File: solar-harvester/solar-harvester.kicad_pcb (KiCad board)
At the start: 2 copper layers, 46.2 x 15.7 mm, 18 parts, among them P1 CONN_2, P2 CONN_2, P3 CONN_2, P4 CONN_6, P5 CONN_6, U1 LTC3588-1

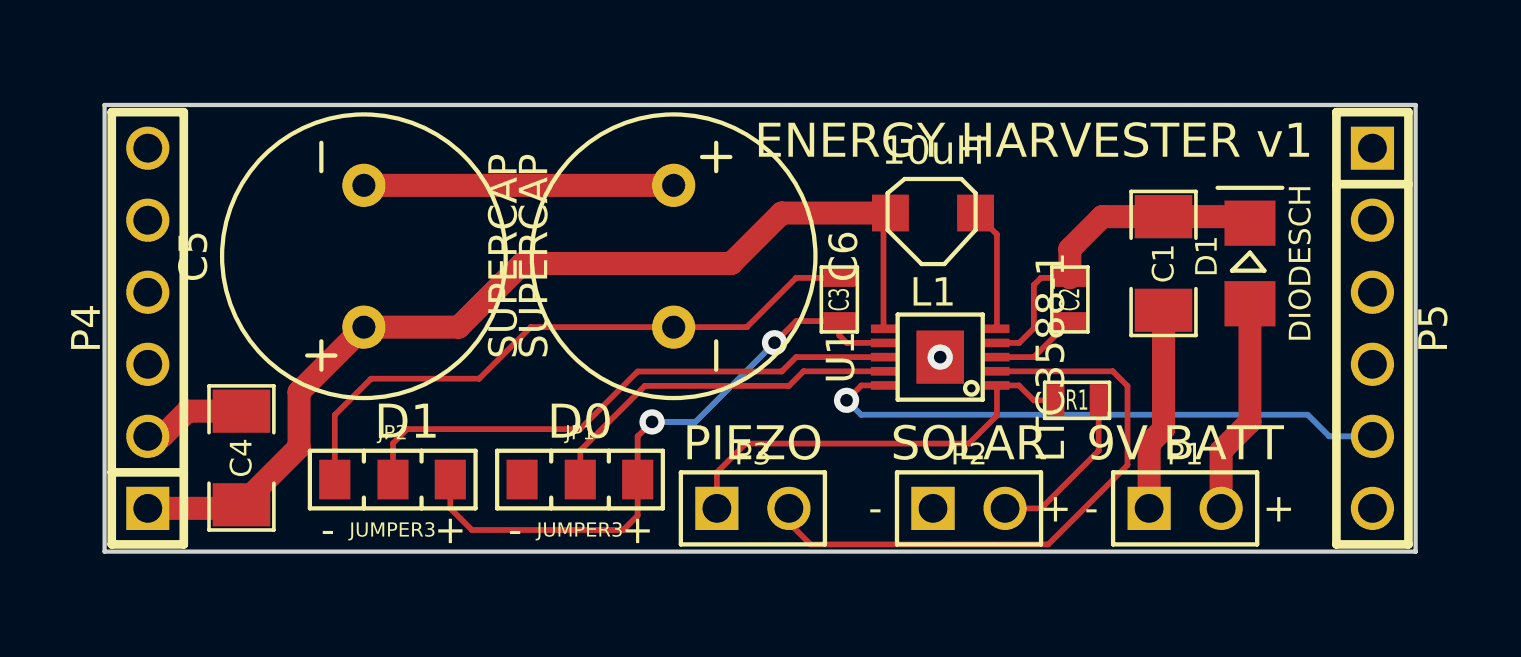
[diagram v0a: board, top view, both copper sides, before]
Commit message: solar-harvester: Add initial PCB layout.
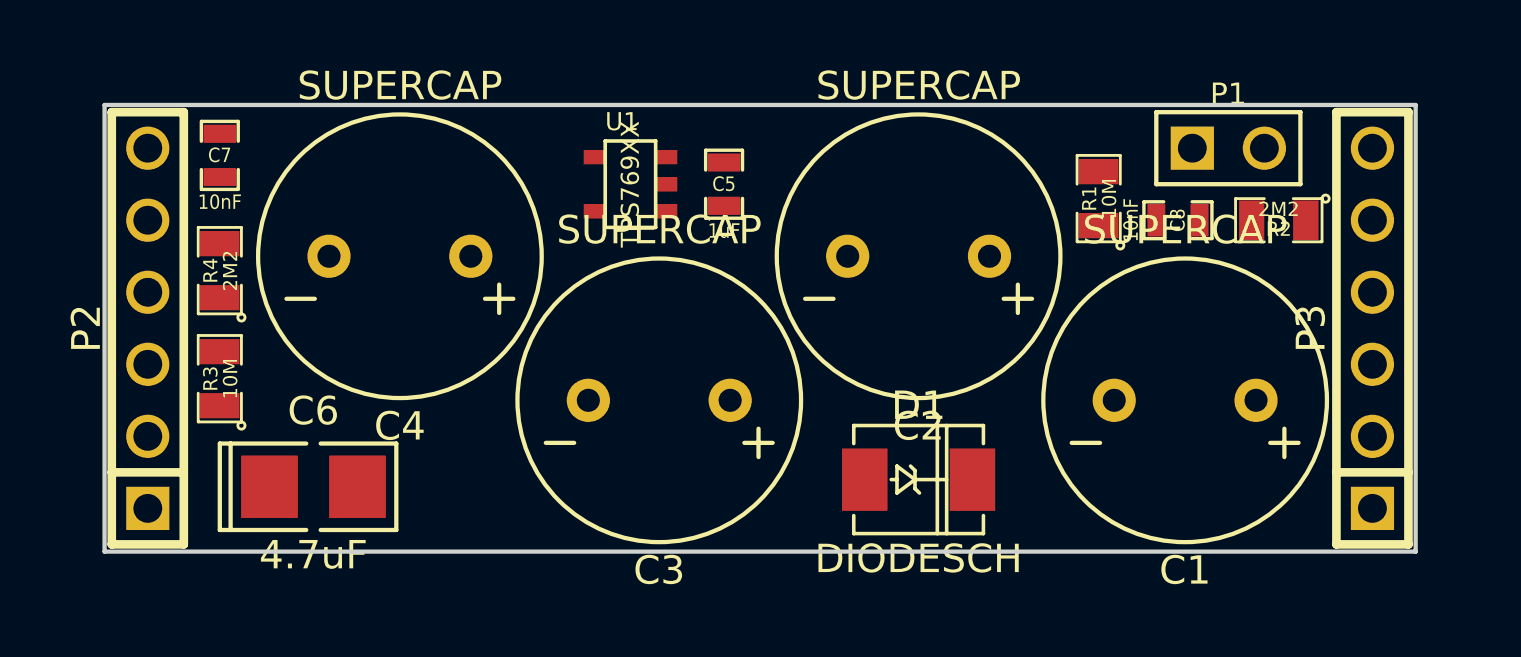
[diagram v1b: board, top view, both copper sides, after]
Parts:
- removed ?: , LOGO_SNOWCAP_BACK
- removed JP1, JP2: JUMPER3, SM0805_JUMPER3
- removed L1: 10uH, INDUCTOR-CDRH2D18-LD
- removed P4, P5: CONN_6, PIN_ARRAY-6X1
- added C7: 10nF, SM0603_Capa, F.Cu at (29.5, 40.9)
- added C8: 10nF, SM0603_Capa, F.Cu at (63.2, 43.2)
- added R2: 2M2, SM0805, F.Cu at (66.8, 43.2)
- added R3: 10M, SM0805, F.Cu at (29.5, 48.8)
- added R4: 2M2, SM0805, F.Cu at (29.5, 45.0)
- C1: value 100uF -> SUPERCAP; footprint SM1206 -> SUPERCAP_ESHSR-0010C0-002R7
- C2: value 1uF -> SUPERCAP; footprint SM0603 -> SUPERCAP_ESHSR-0010C0-002R7
- C3: value 4.7uF -> SUPERCAP; footprint SM0603 -> SUPERCAP_ESHSR-0010C0-002R7
- C4: value 10uF -> SUPERCAP; footprint SM1206 -> SUPERCAP_ESHSR-0010C0-002R7
- C5: value SUPERCAP -> 1uF; footprint SUPERCAP_ESHSR-0010C0-002R7 -> SM0603_Capa
- C6: value SUPERCAP -> 4.7uF; footprint SUPERCAP_ESHSR-0010C0-002R7 -> SM1411_POL
- D1: footprint DIODE-1206 -> DO-214AC(SMA)
- P2, P3: value CONN_2 -> CONN_6; footprint PIN_ARRAY_2X1 -> PIN_ARRAY-6X1
- R1: value 300R -> 10M; footprint SM0603 -> SM0805
- U1: value LTC3588-1 -> TPS769XX; footprint LTC3588-1-MSOP10 -> SOT23-5
- moved P2 29.6 mm to (26.9, 47.0), turned to 90 degrees
- moved P3 22.7 mm to (70.1, 47.0), turned to 90 degrees
- moved C6 15.1 mm to (32.8, 52.6), turned to 0 degrees
- moved D1 13.9 mm to (54.1, 52.3), turned to 0 degrees
- moved C5 13.0 mm to (47.2, 41.9)
- moved P1 12.8 mm to (65.0, 40.6)
- moved U1 12.5 mm to (43.9, 41.9)
- moved C4 9.04 mm to (35.8, 44.5), turned to 180 degrees
- moved C3 7.28 mm to (45.0, 49.5), turned to 180 degrees
- moved R1 7.15 mm to (60.5, 42.4), turned to 90 degrees
- moved C2 5.55 mm to (54.1, 44.5), turned to 180 degrees
- moved C1 4.89 mm to (63.5, 49.5), turned to 180 degrees
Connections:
- C1 pad 1: N-0000023 -> N-0000016
- C1 pad 2: GND -> N-0000015
- C2 pad 1: N-0000023 -> N-0000015
- C2 pad 2: N-0000018 -> N-000002
- C3 pad 1: /VIN2 -> N-000002
- C3 pad 2: GND -> N-0000017
- C4 pad 1: VCC -> N-0000017
- C5 pad 1: VCC -> N-0000016
- C5 pad 2: N-0000014 -> GND
- D1 pad 2: N-0000023 -> N-0000016
- P2 pad 1: GND -> N-0000014
- P2 pad 2: N-0000020 -> GND
- P3 pad 1: N-0000011 -> (no net)
- P3 pad 2: N-0000012 -> /V_MEASURE2
- R1 pad 1: N-0000020 -> N-0000016
- R1 pad 2: N-0000011 -> /V_MEASURE2
- U1 pad 1: N-0000011 -> N-0000016
- U1 pad 2: N-0000012 -> GND
- U1 pad 3: N-0000018 -> GND
- U1 pad 4: N-0000023 -> (no net)
- U1 pad 5: N-0000022 -> N-0000014
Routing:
- net VCC: track 35.8 -> 0.00 mm
- net GND: track 32.9 -> 0.00 mm, vias 1 -> 0
- net /VIN2: track 21.9 -> 0.00 mm, vias 2 -> 0
- net N-0000012: track 21.5 -> 0.00 mm
- net /PGOOD: track 20.6 -> 0.00 mm, vias 1 -> 0
- net N-0000013: track 19.8 -> 0.00 mm
- net N-0000011: track 15.3 -> 0.00 mm
- net N-0000015: track 12.9 -> 0.00 mm
- net N-0000023: track 12.3 -> 0.00 mm
- net N-0000014: track 10.9 -> 0.00 mm
- net N-000003: track 7.41 -> 0.00 mm
- net N-0000020: track 5.92 -> 0.00 mm
- net N-0000022: track 4.39 -> 0.00 mm
- net N-0000018: track 3.10 -> 0.00 mm
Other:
- board text removed: "+"
- board text removed: "-"
- board text removed: "9V BATT"
- board text removed: "D0"
- board text removed: "D1"
- board text removed: "ENERGY HARVESTER v1"
- board text removed: "GND"
- board text removed: "PGOOD"
- board text removed: "PIEZO"
- board text removed: "SOLAR"
- board text removed: "VCC"

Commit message: solar-harvester: Add PCB traces.
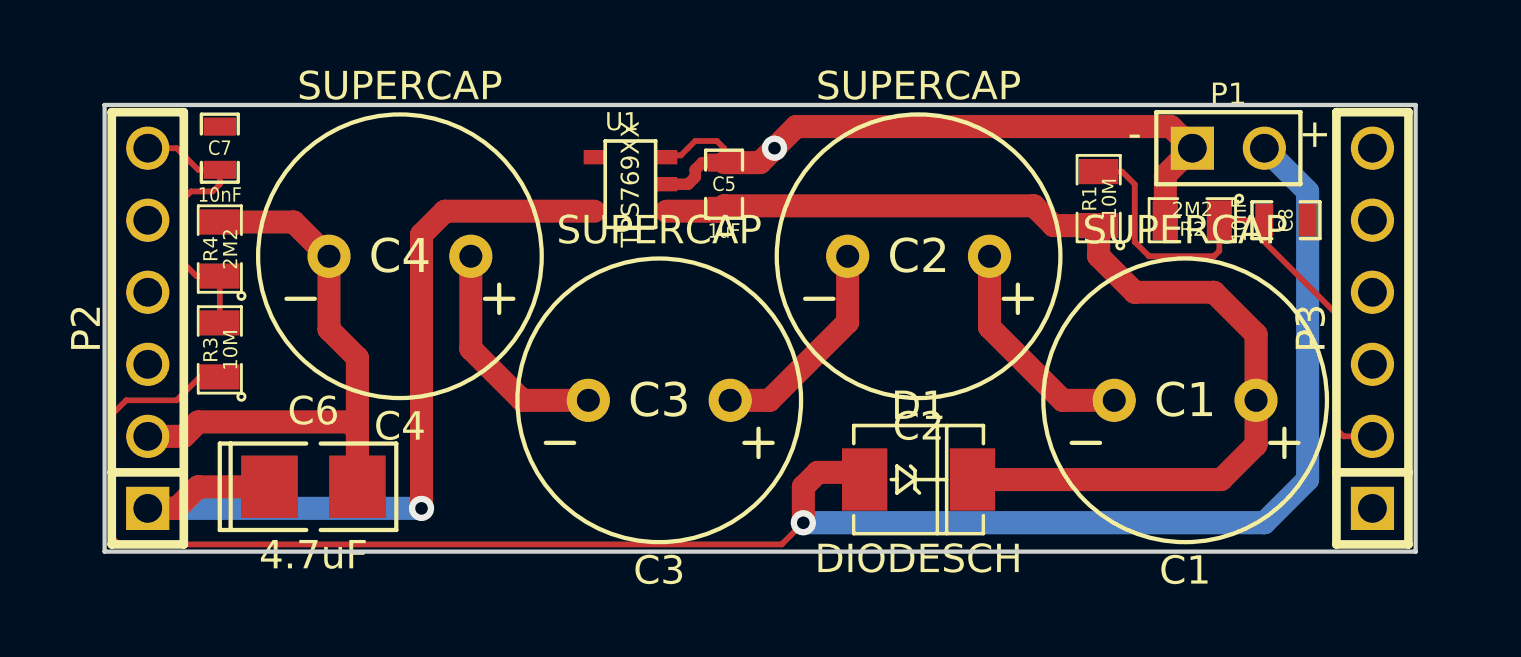
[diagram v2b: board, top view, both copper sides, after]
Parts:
- added ?: , LOGO_SNOWCAP_BACK, B.Cu at (48.8, 46.5)
- moved C8 3.81 mm to (67.1, 43.2)
- moved R2 3.05 mm to (63.8, 43.2)
- moved R3 1.02 mm to (29.5, 47.8)
- moved R4 0.76 mm to (29.5, 44.2)
- moved C7 0.25 mm to (29.5, 40.6)
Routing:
- net N-000003: track 0.00 -> 68.0 mm, vias 0 -> 1
- net GND: track 0.00 -> 48.3 mm, vias 0 -> 1
- net N-0000016: track 0.00 -> 37.8 mm
- net N-0000014: track 0.00 -> 30.3 mm, vias 0 -> 1
- net /V_MEASURE2: track 0.00 -> 19.2 mm
- net /V_MEASURE1: track 0.00 -> 10.2 mm
- net N-0000017: track 0.00 -> 8.16 mm
- net N-0000015: track 0.00 -> 7.97 mm
- net N-000002: track 0.00 -> 7.61 mm
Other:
- board text added: "+"
- board text added: "-"
- board text added: "C1"
- board text added: "C2"
- board text added: "C3"
- board text added: "C4"
- board text added: "SOLAR HARVESTER v1"
- board text added: "V_MEASURE1_SOLAR"
- board text added: "V_MEASURE2_CAPS"
